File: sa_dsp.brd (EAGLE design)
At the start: 150 x 110 mm, 369 parts, among them CN1 uSD, CN2 MINI B USB, CN3 2X5 HEADER, CN4 MINI B USB, CN5 USB A, CN6 MINI B USB, Q3 2N7002, Q4 2N7002, SW1 1825910-7, U1 PGA2311, U10 LME49720, U11 PGA2311, U12 LME49720, U13 LME49720, U14 PCM1754, U15 LME49720, U16 PGA2311, U17 LME49720, U18 LME49720, U19 PCM1754, U2 LM317, U20 LME49720, U21 7 SEG, U22 74HC164A, U23 PCM2707, U24 PCM2707, U25 7 SEG, U26 74HC164A, U27 LM337, U28 LM317, U29 7 SEG, U3 OSD3358-512M-BSM, U30 74HC164A, U31 100MHz, U32 USBLC6-2SC6, U33 FT230X, U34 USBLC6-2SC6, U35 USBLC6-2SC6, U36 USBLC6-2SC6, U37 2 PORT HUB, U4 LME49720, U5 LME49720, U6 10CL016YF484C6G, U7 7 SEG, U8 74HC164A, U9 PCM1754

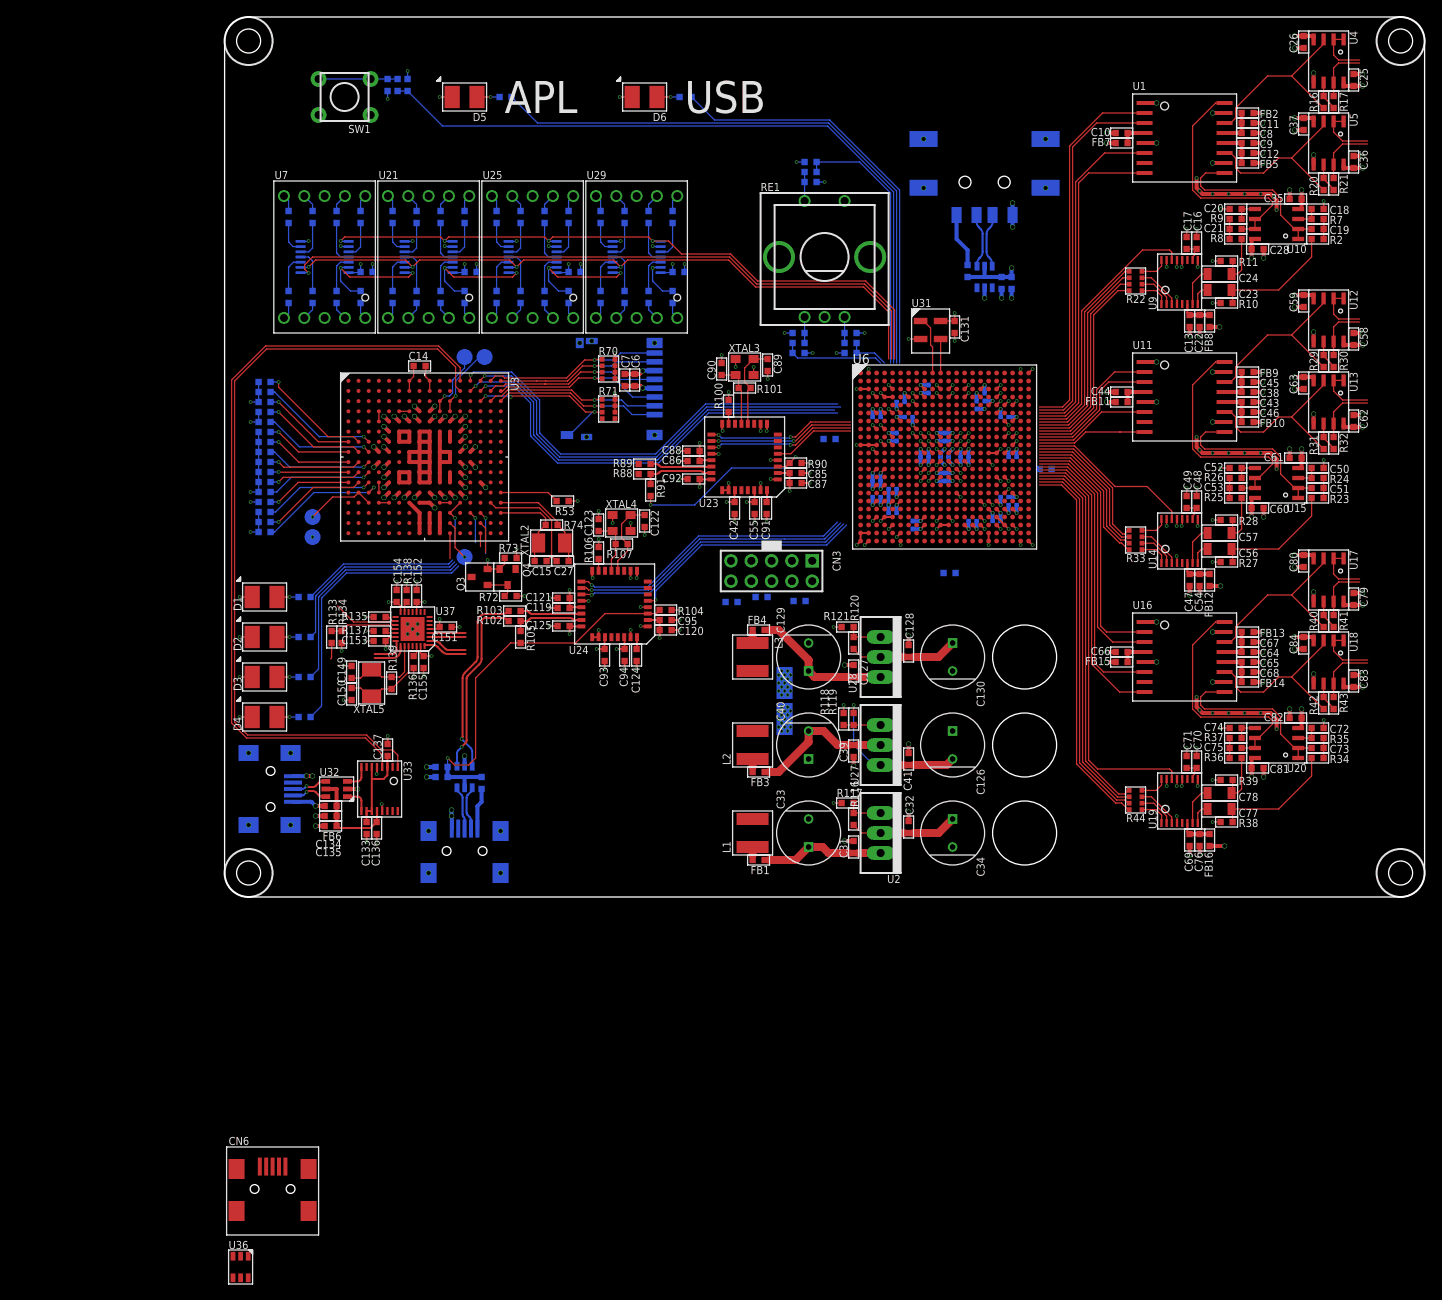
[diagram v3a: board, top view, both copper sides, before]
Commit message: USB routed
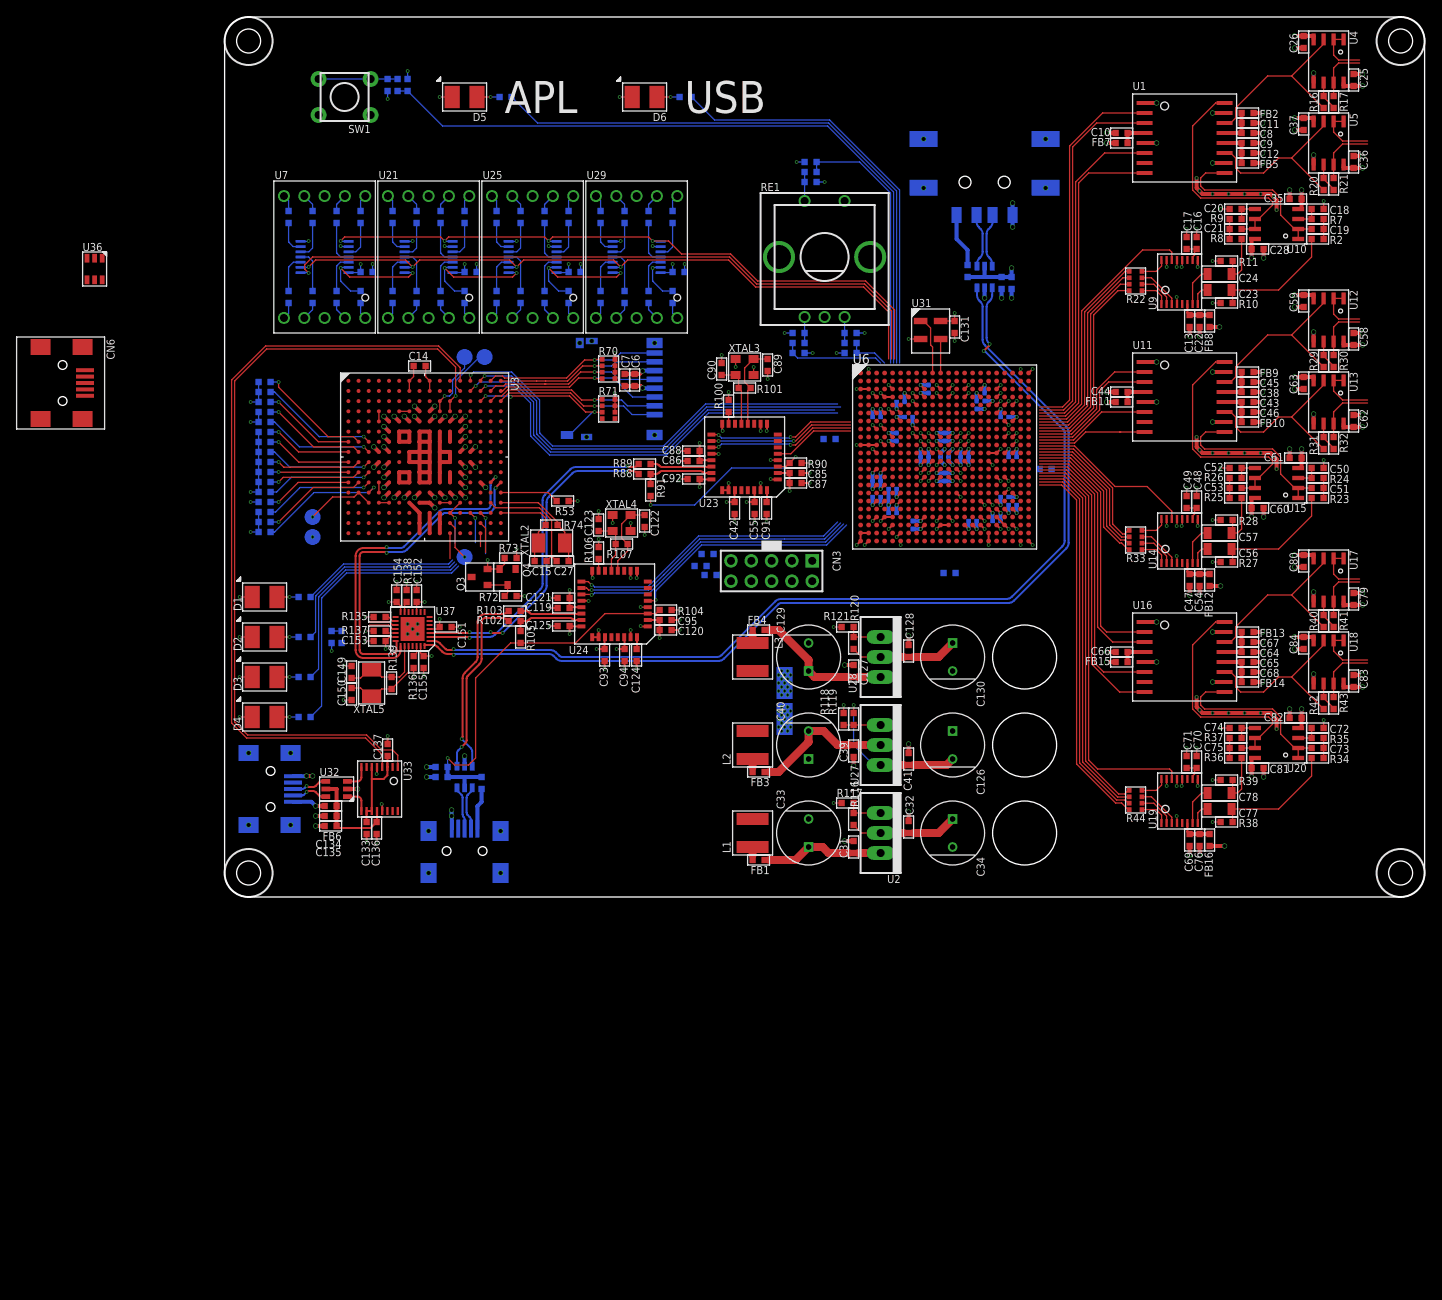
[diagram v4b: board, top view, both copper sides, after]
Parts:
- moved U36 126.1 mm to (-16.2, 78.5)
- moved CN6 104.1 mm to (-20.2, 64.2), turned to 270 degrees
- moved R15 12.9 mm to (60.4, 42.9)
- moved R14 6.94 mm to (60.8, 40.2)
- moved R84 5.94 mm to (59.5, 41.4)
- moved R133 1.25 mm to (14.6, 32.5), flipped to the bottom
- moved R134 1.25 mm to (13.4, 32.5), flipped to the bottom
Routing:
- net USB_OUT0_DN: track 5.60 -> 123.8 mm, vias 0 -> 1
- net USB_OUT0_DP: track 4.88 -> 122.5 mm, vias 0 -> 3
- net OSD_USB1_DP: track 4.16 -> 42.8 mm, vias 0 -> 2
- net USB_OUT1_DN: track 4.50 -> 41.5 mm, vias 0 -> 2
- net USB_OUT1_DP: track 4.50 -> 41.2 mm, vias 0 -> 4
- net OSD_USB1_DM: track 4.21 -> 40.7 mm, vias 0 -> 2
- net USB_RESET: track 8.23 -> 3.41 mm
- net N$229: track 8.52 -> 4.71 mm
- net 5VUSB: track 50.8 -> 48.8 mm
- net OSD_SPI_SCLK: track 56.0 -> 55.2 mm
- net OSD_SPI_MOSI: track 53.9 -> 53.1 mm
- net OSD_SPI_MISO: track 55.0 -> 54.2 mm
- net OSD_SPI_CS_FPGA: track 54.5 -> 53.7 mm

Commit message: Working on PSUs
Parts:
- added C142, C157: 47uF 25V, CAPACITORS:1206
- added C147: 10nF 50V, CAPACITORS:0603
- added C148: 47uF 10V, CAPACITORS:1206
- added C156: 100nF 16V, CAPACITORS:0603
- added C158: 100nF 100V, CAPACITORS:0603
- added D8: BC560, DIODES:SMC
- added L5: 47uH 3.1A, INDUCTORS:SRR1210
- added R128: 160k, r_0603:0603
- added U39: LM22670, ICs:SO8_PP
- moved CN6 41.5 mm to (5.75, 96.6), flipped to the bottom, turned to 90 degrees
- moved U36 36.2 mm to (16.8, 93.4), flipped to the bottom, turned to 90 degrees
- moved C138 10.0 mm to (27.1, 25.0)
- moved C139 10.0 mm to (27.1, 26.2)
- moved CN4 10.0 mm to (30.0, 15.8)
- moved FB17 10.0 mm to (32.1, 24.2)
- moved U34 10.0 mm to (30.0, 25.0)
- moved R133 2.30 mm to (15.1, 34.8), turned to 270 degrees
- moved R134 2.30 mm to (13.9, 34.8), turned to 270 degrees
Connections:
- removed net N$207: U3.M14, U3.M15
- new net N$212: C147.1, U39.1
- new net N$213: C147.2, D8.K, L5.1, U39.8
- new net N$236: R128.2, U39.3
- new net OSD_USB1_VBUS: R133.1, U3.M14, U3.M15
- net 15VD_UNREG: now also C142.1, C157.1, C158.2, U39.7
- net 5V: now also C148.2, C156.2, L5.2, U39.4
- net 5VUSB: no longer R133.1
- net GND: now also C142.2, C148.1, C156.1, C157.2, C158.1, D8.A, R128.1, U39.6, U39.PAD
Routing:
- net GND: track 264.3 -> 306.7 mm, vias 261 -> 283
- net OSD_USB1_VBUS: track 0.00 -> 35.1 mm, vias 0 -> 1
- net N$213: track 0.00 -> 19.0 mm
- net 5V: track 131.6 -> 147.6 mm
- net N$173: track 22.8 -> 12.8 mm
- net N$172: track 23.6 -> 13.6 mm
- net 5VUSB: track 48.8 -> 39.9 mm
- net N$229: track 4.71 -> 7.71 mm, vias 0 -> 1
- net N$212: track 0.00 -> 1.93 mm
- net N$236: track 0.00 -> 1.68 mm
- added copper zone on layer 1, net 15VD_UNREG
- added copper zone on layer 1, net 5V
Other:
- outline, holes or cut-outs redrawn

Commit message: Progress on DSP
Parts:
- moved R14 12.4 mm to (72.6, 43.8), turned to 270 degrees
- moved R15 7.18 mm to (67.5, 43.8), turned to 90 degrees
- moved R84 3.73 mm to (62.4, 43.8), turned to 90 degrees
- moved R91 3.13 mm to (50.4, 49.6), turned to 0 degrees
- moved R88 2.92 mm to (50.4, 50.9)
- moved R89 2.92 mm to (50.4, 52.1)
- moved CN3 1.15 mm to (67.5, 40.0)
- moved R85 0.28 mm to (75.8, 57.5)
- moved R87 0.12 mm to (90.8, 40.5)
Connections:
- removed net STM_AM_UART_RX: U3.B11
- removed net STM_AM_UART_TX: U3.A11
- new net OSD_FPGA_GPIO0: U3.T12, U6.F1
- new net OSD_FPGA_GPIO1: U3.R12, U6.E1
- new net OSD_FPGA_GPIO2: U3.P12, U6.E2
- new net OSD_FPGA_GPIO3: U3.T13, U6.M1
- new net OSD_FPGA_GPIO4: U3.R13, U6.F2
- new net OSD_FPGA_GPIO5: U3.T15, U6.N1
- new net OSD_FPGA_GPIO6: U3.R15, U6.M2
- new net OSD_FPGA_GPIO7: U3.T16, U6.N2
- net 5V: no longer C148.2, C156.2, L5.2, U39.4
- net 5VD: now also C148.2, C156.2, L5.2, U39.4
- net OSD_SPI_CS_FPGA: now also U6.B1
- net OSD_SPI_MISO: now also U6.D2
- net OSD_SPI_MOSI: now also U6.D1
- net OSD_SPI_SCLK: now also U6.B2
- net PCM_I2S_BCLK_BB: now also U6.G2
- net PCM_I2S_BCLK_EXT: now also U6.W2
- net PCM_I2S_DOUT_BB: now also U6.H1
- net PCM_I2S_DOUT_EXT: now also U6.W1
- net PCM_I2S_LRCLK_BB: now also U6.H2
- net PCM_I2S_LRCLK_EXT: now also U6.Y1
- net PCM_I2S_MCLK_BB: now also U6.G1
- net PCM_I2S_MCLK_EXT: now also U6.T2
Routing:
- net OSD_FPGA_GPIO3: track 0.00 -> 61.3 mm, vias 0 -> 2
- net OSD_FPGA_GPIO4: track 0.00 -> 60.6 mm, vias 0 -> 2
- net OSD_FPGA_GPIO0: track 0.00 -> 60.4 mm, vias 0 -> 2
- net OSD_FPGA_GPIO2: track 0.00 -> 59.4 mm, vias 0 -> 2
- net OSD_FPGA_GPIO5: track 0.00 -> 59.4 mm, vias 0 -> 2
- net OSD_FPGA_GPIO6: track 0.00 -> 58.6 mm, vias 0 -> 2
- net OSD_FPGA_GPIO1: track 0.00 -> 58.4 mm, vias 0 -> 2
- net OSD_FPGA_GPIO7: track 0.00 -> 54.3 mm, vias 0 -> 2
- net 5VD: track 35.0 -> 89.0 mm, vias 3 -> 24
- net CONF_JTAG_TDI: track 0.00 -> 32.2 mm, vias 0 -> 2
- net CONF_JTAG_TCK: track 0.00 -> 29.4 mm, vias 0 -> 2
- net CONF_JTAG_TDO: track 0.00 -> 23.6 mm, vias 0 -> 2
- net CONF_JTAG_TMS: track 0.00 -> 22.6 mm, vias 0 -> 1
- net 5V: track 147.6 -> 131.6 mm
- net AM_PMIC_PGOOD: track 7.01 -> 22.9 mm
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- added copper zone on layer 1, net 5VD
- added copper zone on layer 3, net 5VD
- removed copper zone on layer 1, net 5V

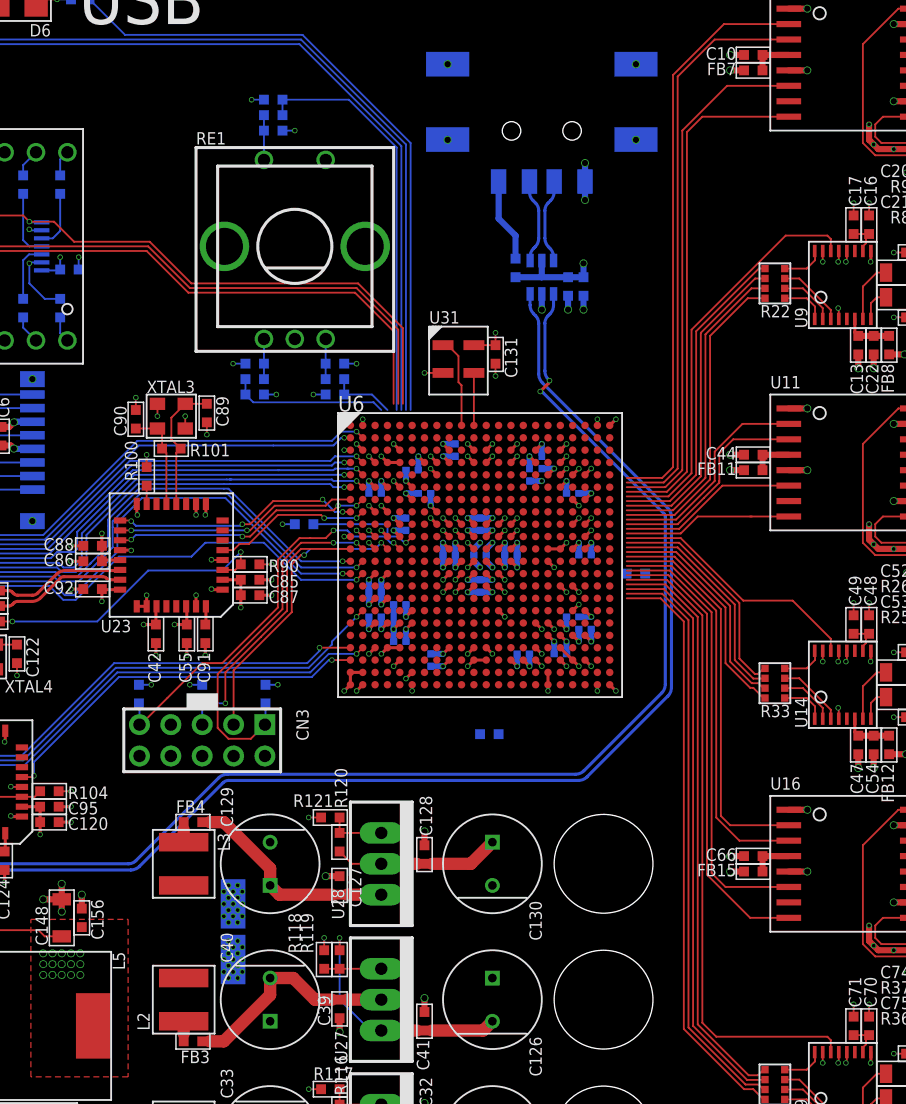
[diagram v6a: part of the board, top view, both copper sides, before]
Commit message: PSUs done for the FPGA
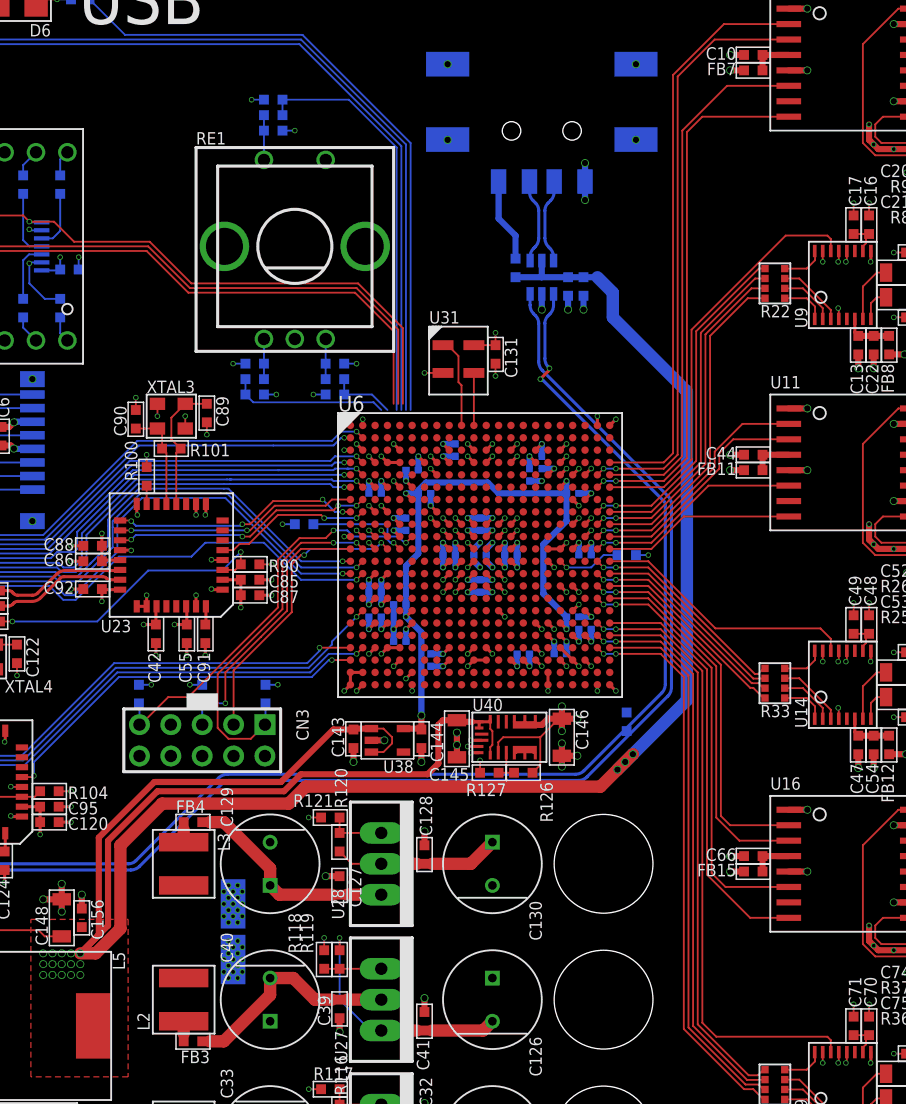
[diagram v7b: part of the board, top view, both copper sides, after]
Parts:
- added C143: 1uF 25V, CAPACITORS:0603
- added C144: 2.2uF 25V, CAPACITORS:0603
- added C145, C146: 22uF 10V, CAPACITORS:1206
- added R126, R127: 200k, r_0603:0603
- added U38: TPS70925, ICs:SOT23-5
- added U40: MPM3820, ICs:MPM3820
- moved R87 11.2 mm to (101.9, 41.5), turned to 270 degrees
- moved R86 1.68 mm to (101.9, 55.0)
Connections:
- new net N$207: U40.4, U40.45, U40.5, U40.56, U40.6
- new net N$210: R126.1, R127.2, U40.3
- net 1V2: now also C146.2, R126.2, U40.2, U40.7, U40.78, U40.8, U40.89, U40.9
- net 2V5: now also C144.2, U38.5
- net 5VD: now also C143.2, C145.2, U38.1, U38.3, U40.1, U40.12, U40.13, U40.14
- net DAC0_I2S_BCLK: now also U6.W21
- net DAC0_I2S_DATA: now also U6.W22
- net DAC0_I2S_LRCLK: now also U6.V21
- net DAC0_I2S_SCLK: now also U6.V22
- net DAC0_MUTE: now also U6.U21
- net DAC1_I2S_BCLK: now also U6.P22
- net DAC1_I2S_DATA: now also U6.N21
- net DAC1_I2S_LRCLK: now also U6.N22
- net DAC1_I2S_SCLK: now also U6.M21
- net DAC1_MUTE: now also U6.M22
- net DAC2_I2S_BCLK: now also U6.J22
- net DAC2_I2S_DATA: now also U6.J21
- net DAC2_I2S_LRCLK: now also U6.H22
- net DAC2_I2S_SCLK: now also U6.H21
- net DAC2_MUTE: now also U6.F22
- net GND: now also C143.1, C144.1, C145.1, C146.1, R127.1, U38.2, U40.16, U40.17, U40.18
- net PGA0_!CS: now also U6.P21
- net PGA0_!MUTE: now also U6.U22
- net PGA0_SCLK: now also U6.R21
- net PGA0_SDI: now also U6.R22
- net PGA1_!CS: now also U6.K21
- net PGA1_!MUTE: now also U6.L22
- net PGA1_SCLK: now also U6.L21
- net PGA1_SDI: now also U6.K22
- net PGA2_!CS: now also U6.D22
- net PGA2_!MUTE: now also U6.F21
- net PGA2_SCLK: now also U6.E22
- net PGA2_SDI: now also U6.E21
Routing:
- net 5VD: track 89.0 -> 280.2 mm, vias 24 -> 26
- net 2V5: track 6.83 -> 51.8 mm, vias 4 -> 5
- net 1V2: track 32.0 -> 49.8 mm, vias 27 -> 30
- net GND: track 306.5 -> 318.4 mm, vias 287 -> 299
- net CONF_CONFDN: track 0.00 -> 5.25 mm, vias 0 -> 1
- net DAC0_I2S_DATA: track 47.2 -> 44.1 mm
- net PGA1_SCLK: track 14.6 -> 17.6 mm, vias 0 -> 2
- net DAC0_I2S_SCLK: track 47.2 -> 44.2 mm
- net N$210: track 0.00 -> 2.88 mm
- net PGA0_!MUTE: track 37.0 -> 34.1 mm
- net PGA0_SDI: track 32.2 -> 29.8 mm
- net PGA1_!CS: track 17.7 -> 20.0 mm, vias 0 -> 2
- net DAC1_I2S_BCLK: track 18.6 -> 16.3 mm
- net DAC2_I2S_DATA: track 25.6 -> 27.8 mm, vias 0 -> 2
- net DAC1_I2S_LRCLK: track 18.2 -> 16.1 mm
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
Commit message: Progress
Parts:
- added C159, C160: 22uF 10V, CAPACITORS:1206
- added D10, D7: CG0603MLC, DIODES:0603_POLAR
- added D11, D9: B0540W, DIODES:SOD-123
- added Q1, Q2: 2N7002, TRANSISTORs:SOT23-3
- added R129, R131, R132: 100k, r_0603:0603
- added R130: 22k, r_0603:0603
- added TP10, TP11, TP12, TP8, TP9: TEST_POINT_SQUARE, MISC:OSPREY_HSS_PAD
- added TP13, TP14, TP15, TP16: 2MM_TEST_POINT, MISC:2MM_TEST_PAD
- added U41: MPM3820, ICs:MPM3820
- R126, R127: value 200k -> 22k
- moved TP7 19.0 mm to (11.0, 42.5), turned to 180 degrees
- moved U36 3.77 mm to (13.0, 93.0), turned to 180 degrees
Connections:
- new net IO_AUDIO_RLY_EN: Q2.1, R132.2
- new net N$211: R129.1, R130.2, U41.3
- new net N$237: D10.K, D11.A, Q2.2, TP16.1
- new net PSU_AMP_PWR_EN: Q1.1, R131.2
- net 15VA+_UNREG: now also TP10.1
- net 15VA-_UNREG: now also TP12.1
- net 15VD_UNREG: now also D11.K, D9.K, TP13.1, TP15.1, TP8.1
- net 3V3: now also C160.2, R129.2, U41.2, U41.7, U41.78, U41.8, U41.89, U41.9
- net 5VD: now also C159.2, U41.1, U41.12, U41.13, U41.14
- net AGND: now also TP11.1
- net GND: now also C159.1, C160.1, D10.A, D7.A, Q1.3, Q2.3, R130.1, R131.1, R132.1, TP9.1, U41.16, U41.17, U41.18
- net N$207: now also D7.K, D9.A, Q1.2, TP14.1; no longer U40.4, U40.45, U40.5, U40.56, U40.6
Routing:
- net OSD_DEBUG_USB_DP: track 0.00 -> 59.4 mm, vias 0 -> 1
- net OSD_DEBUG_USB_DM: track 0.00 -> 58.6 mm, vias 0 -> 1
- net 15VD_UNREG: track 0.00 -> 39.6 mm, vias 0 -> 6
- net 3V3: track 122.5 -> 153.7 mm, vias 76 -> 82
- net 5VD: track 280.2 -> 307.1 mm
- net GND: track 318.4 -> 337.1 mm, vias 299 -> 315
- net AGND: track 123.6 -> 141.5 mm
- net AM_WARM_!RST: track 13.1 -> 26.4 mm
- net 15VA+_UNREG: track 0.00 -> 12.5 mm, vias 0 -> 3
- net 15VA-_UNREG: track 0.00 -> 11.8 mm, vias 0 -> 3
- net AM_PMIC_PGOOD: track 22.9 -> 19.8 mm
- net N$211: track 0.00 -> 2.88 mm
- net AM_I2C0_SCL: track 8.43 -> 10.6 mm
- net N$207: track 2.11 -> 0.00 mm
- net AM_I2C0_SDA: track 8.98 -> 10.9 mm
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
